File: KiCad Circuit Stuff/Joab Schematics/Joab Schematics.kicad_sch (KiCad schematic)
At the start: 57 parts, among them J1 Conn_02x16_Odd_Even, J2 Conn_01x02, Q1 S8550, Q2 MMBT3904, U1 MT3608, U2 AMS1117-3.3, U3 TP4056, U4 INA219AIDCNR, U6 TS5A3159DCKR, U7 TPS5430DDAR

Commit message: Chose all passive components, added test points to all
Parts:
- removed Q1: S8550, Package_TO_SOT_SMD:SOT-23, symbol Transistor_BJT:S8550
- removed Q2: MMBT3904, Package_TO_SOT_SMD:SOT-23, symbol Transistor_BJT:MMBT3904
- removed R8: 2k, Resistor_SMD:R_0402_1005Metric_Pad0.72x0.64mm_HandSolder, symbol Device:R_Small_US
- removed R9: 1000k, Resistor_SMD:R_0402_1005Metric_Pad0.72x0.64mm_HandSolder, symbol Device:R_Small_US
- removed TP10, TP3, TP4, TP5, TP9: TestPoint, TestPoint:TestPoint_Pad_2.5x2.5mm, symbol Connector:TestPoint
- added 9-5V_R1_TP1: 9-5V R1 TP, TestPoint:TestPoint_Pad_2.5x2.5mm, symbol Connector:TestPoint
- added 9-5V_R2_TP1: 9-5V R2 TP, TestPoint:TestPoint_Pad_2.5x2.5mm, symbol Connector:TestPoint
- added 9-5V_VSense_TP1: 9-5V VSense TP, TestPoint:TestPoint_Pad_2.5x2.5mm, symbol Connector:TestPoint
- added CHRG_SelectR1_TP1, CHRG_SelectR1_TP2, CHRG_SelectR2_TP1, CHRG_SelectR2_TP2, CHRG_VinR_TP1, CHRG_VinR_TP2, Shunt_TP1, Shunt_TP2: TestPoint, TestPoint:TestPoint_Pad_2.5x2.5mm, symbol Connector:TestPoint
- added R16: 2.2k, Resistor_SMD:R_0402_1005Metric_Pad0.72x0.64mm_HandSolder, symbol Device:R_Small_US
- 5V_FB_TP1: renamed from TP7; value TestPoint -> 5V FB TP
- 5V_R1_TP1: renamed from TP6; value TestPoint -> ~
- 5V_R2_TP1: renamed from TP8; value TestPoint -> 5V R2 TP
- L_TP_1: renamed from TP2; value L TP 1 -> ~
- L_TP_2: renamed from TP1; value L TP 2 -> ~
- R10, R11: footprint Resistor_SMD:R_0402_1005Metric_Pad0.72x0.64mm_HandSolder -> Resistor_SMD:R_0603_1608Metric_Pad0.98x0.95mm_HandSolder; LCSC (none) -> C21189
- R12: value 0.1R -> 100m; LCSC (none) -> C7467250
- R13: LCSC (none) -> C4109
- R14: value 5.5k -> 3.3k; LCSC (none) -> C25890
- R15: value 1.5R -> 2.2R; footprint Resistor_SMD:R_0402_1005Metric_Pad0.72x0.64mm_HandSolder -> Resistor_SMD:R_0603_1608Metric_Pad0.98x0.95mm_HandSolder; LCSC (none) -> C22939
- R7: value 5.5k -> 4.7R; footprint Resistor_SMD:R_0402_1005Metric_Pad0.72x0.64mm_HandSolder -> Resistor_SMD:R_0603_1608Metric_Pad0.98x0.95mm_HandSolder; LCSC (none) -> C23164
- renumbered TP13 to 3V3_TP1, TP12 to 5V_TP1, TP11 to 9V_TP1, TP15 to BAT_TP1, TP14 to GND_TP1
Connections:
- net Battery: no longer J1.14 (Pin_14)
- net Battery_In: now also J1.14 (Pin_14), Shunt_TP1.1
- net Battey_Charger_VDD: now also 9-5V_R1_TP1.1
- net GND: now also 9-5V_R2_TP1.1, CHRG_SelectR1_TP2.1, CHRG_SelectR2_TP2.1, CHRG_VinR_TP2.1, R16.2; no longer R14.2
- net at C9.1, R15.1: now also R7.1, CHRG_VinR_TP1.1
- net at R4.1, R5.2, U7.4 (VSENSE): now also 9-5V_VSense_TP1.1
- net at R13.1, U6.1 (NO): now also CHRG_SelectR2_TP1.1
- net at R14.1, U6.3 (NC): now also CHRG_SelectR1_TP1.1
- net Battery_Out renamed Battery_Out_After_Switch
- net Battery_Out_After_Switch: no longer C2.2, JP2.2 (B), R10.1, R12.1, U3.5 (BAT)
- new net: R14.2, R16.1
- new net Battery_Out_Before_Switch: C2.2, JP2.2 (B), R10.1, R12.1, Shunt_TP2.1, U3.5 (BAT)
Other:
- note added: "Notes"
- note removed: "CHANGE THESE RESISTORS"
- note removed: "Cange this resistor"
- note removed: "JOAB YOUR SHIT HERE"
- note removed: "RESISTORS FROM U3-> INA"
- moved on the sheet: 5V_R1_TP1, 5V_R2_TP1, C1, C4, D1, L1, L_TP_1, L_TP_2, R1, R13, R14, R2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

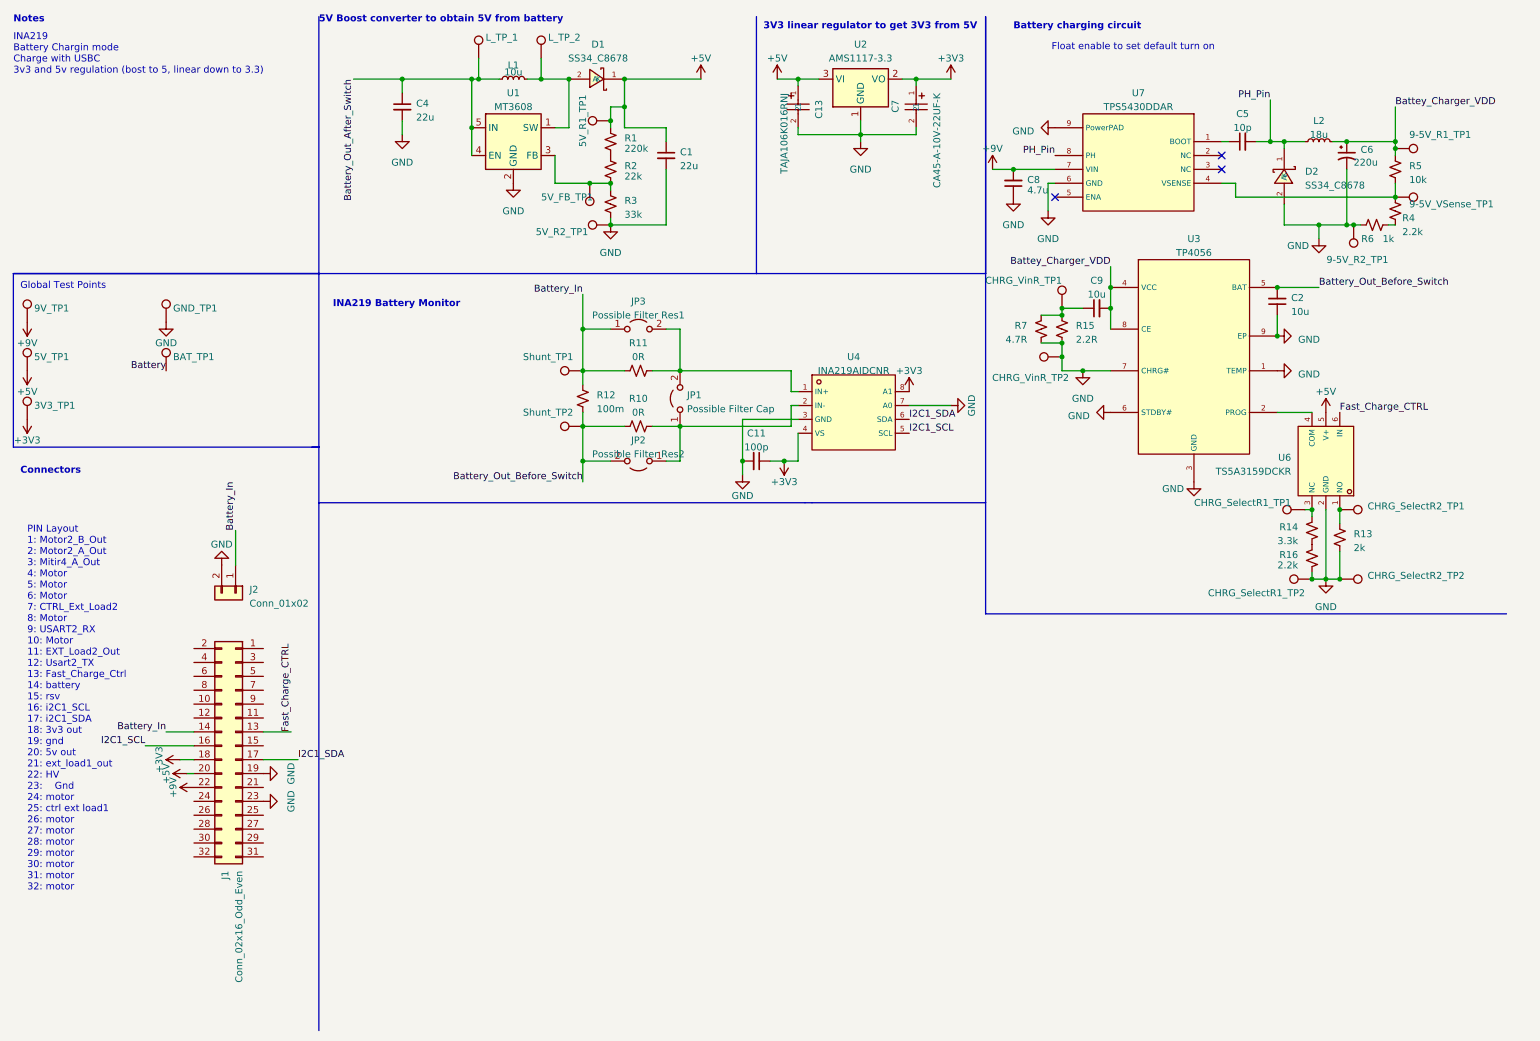
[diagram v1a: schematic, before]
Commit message: Added some lables in Joab Schematic
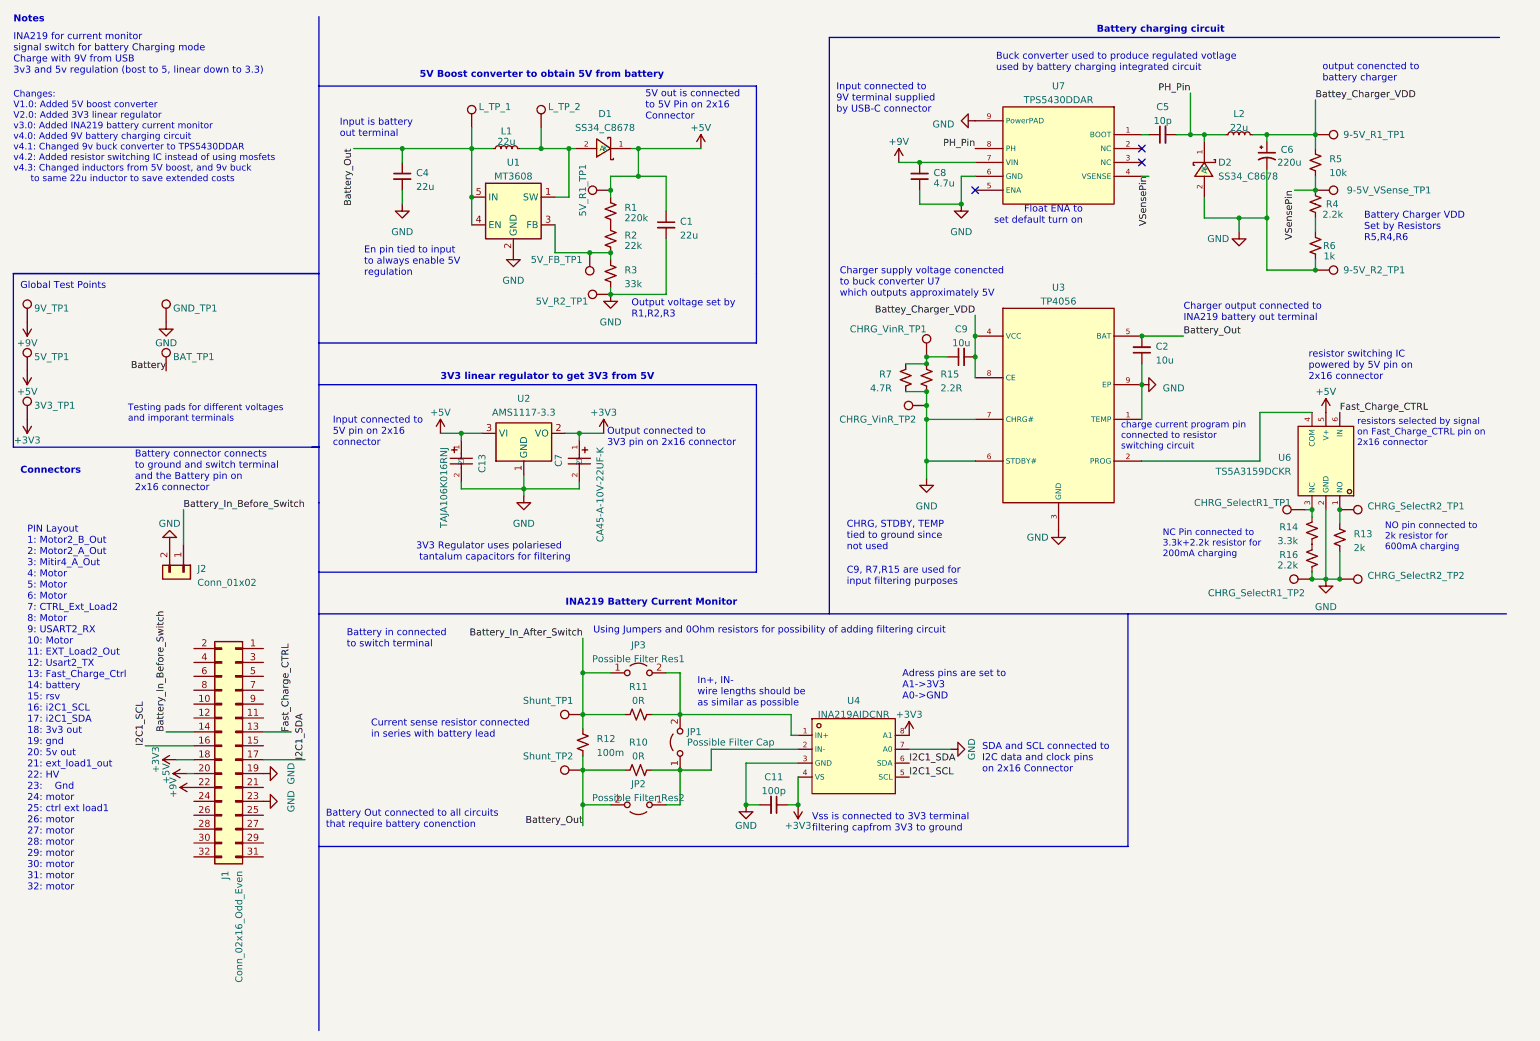
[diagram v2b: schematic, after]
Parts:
- L1: value 10u -> 22u; footprint Inductor_SMD:L_Changjiang_FNR4030S -> Inductor_SMD:L_Sunlord_SWPA6045S; LCSC C167879 -> C83454
- L2: value 18u -> 22u; footprint Inductor_SMD:L_Changjiang_FNR4030S -> Inductor_SMD:L_Sunlord_SWPA6045S; LCSC C167882 -> C83454
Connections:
- net Battery_Out_Before_Switch is gone; now on net Battery_Out: C2.2, JP2.2 (B), R10.1, R12.1, Shunt_TP2.1, U3.5 (BAT)
- net VSensePin: now reaches 9-5V_VSense_TP1.1, R4.1, R5.2, U7.4 (VSENSE)
- net Battery_In renamed Battery_In_After_Switch
- net Battery_In_After_Switch: no longer J1.14 (Pin_14), J2.1 (Pin_1)
- net Battery_Out_After_Switch renamed Battery_Out
- new net Battery_In_Before_Switch: J1.14 (Pin_14), J2.1 (Pin_1)
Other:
- note added: "3V3 Regulator uses polariesed tantalum capacitors for filtering"
- note added: "5V out is connected to 5V Pin on 2x16 Connector"
- note added: "Adress pins are set to A1->3V3 A0->GND"
- note added: "Battery Charger VDD Set by Resistors R5,R4,R6"
- note added: "Battery Out connected to all circuits that require battery conenction"
- note added: "Battery connector connects to ground and switch terminal and the Battery pin on 2x16 connector"
- note added: "Battery in connected to switch terminal"
- note added: "Buck converter used to produce regulated votlage used by battery charging integrated circuit"
- note added: "C9, R7,R15 are used for input filtering purposes"
- note added: "CHRG, STDBY, TEMP tied to ground since not used"
- note added: "Changes: V1.0: Added 5V boost converter V2.0: Added 3V3 linear regulator v3.0: Added INA219 battery current monitor v4.0: Added 9V battery charging circuit v4.1: Changed 9v buck converter to TPS5430DDAR v4.2: Added resistor switching IC instead of using mosfets v4.3: Changed inductors from 5V boost, and 9v buck to same 22u inductor to save extended costs"
- note added: "Charger output connected to INA219 battery out terminal"
- note added: "Charger supply voltage conencted to buck converter U7 which outputs approximately 5V"
- note added: "Current sense resistor connected in series with battery lead"
- note added: "En pin tied to input to always enable 5V regulation"
- note added: "Float ENA to set default turn on"
- note added: "INA219 Battery Current Monitor"
- note added: "INA219 for current monitor signal switch for battery Charging mode Charge with 9V from USB 3v3 and 5v regulation (bost to 5, linear down to 3.3)"
- note added: "In+, IN- wire lengths should be as similar as possible"
- note added: "Input connected to 5V pin on 2x16 connector"
- note added: "Input connected to 9V terminal supplied by USB-C connector"
- note added: "Input is battery out terminal"
- note added: "NC Pin connected to 3.3k+2.2k resistor for 200mA charging"
- note added: "NO pin connected to 2k resistor for 600mA charging"
- note added: "Output connected to 3V3 pin on 2x16 connector"
- note added: "Output voltage set by R1,R2,R3"
- note added: "SDA and SCL connected to I2C data and clock pins on 2x16 Connector"
- note added: "Testing pads for different voltages and imporant terminals"
- note added: "Using Jumpers and 0Ohm resistors for possibility of adding filtering circuit"
- note added: "Vss is connected to 3V3 terminal filtering capfrom 3V3 to ground"
- note added: "charge current program pin connected to resistor switching circuit"
- note added: "output conencted to battery charger"
- note added: "resistor switching IC powered by 5V pin on 2x16 connector"
- note added: "resistors selected by signal on Fast_Charge_CTRL pin on 2x16 connector"
- note removed: "Float enable to set default turn on"
- note removed: "INA219 Battery Chargin mode Charge with USBC 3v3 and 5v regulation (bost to 5, linear down to 3.3)"
- note removed: "INA219 Battery Monitor"
- title: Joab PCP Work -> Joab PCP schematic
- moved on the sheet: 5V_FB_TP1, 5V_R1_TP1, 5V_R2_TP1, 9-5V_R1_TP1, 9-5V_R2_TP1, 9-5V_VSense_TP1, C1, C11, C13, C2, C4, C5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

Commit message: Added ReadMe and other minor changes
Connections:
- net +3V3: now also J1.17 (Pin_17); no longer J1.18 (Pin_18)
- net +5V: now also J1.19 (Pin_19); no longer J1.20 (Pin_20)
- net +9V: now also J1.21 (Pin_21); no longer J1.22 (Pin_22)
- net Battery_In_Before_Switch: now also J1.13 (Pin_13); no longer J1.14 (Pin_14)
- net Fast_Charge_CTRL: now also J1.14 (Pin_14); no longer J1.13 (Pin_13)
- net GND: now also J1.20 (Pin_20), J1.24 (Pin_24); no longer J1.19 (Pin_19), J1.23 (Pin_23)
- net I2C1_SCL: now also J1.15 (Pin_15); no longer J1.16 (Pin_16)
- net I2C1_SDA: now also J1.18 (Pin_18); no longer J1.17 (Pin_17)
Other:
- note added: "PS PIN -> MM PIN Layout NB! Not same as power board pin header 2->1: MOTOR2_B_OUT 1->2: MOTOR2_A_OUT 4->3: MMOTOR4_A_OUT 3->4: MOTOR2_CTRL1 6->5: MOTOR4_B_OUT 5->6: MOTOR2_CTRL2 8->7: CTRL_EXT_LOAD2 7->8: MOTOR4_CTRL1 10->9: USART2_RX 9->10: MOTOR4_CTRL2 12->11: EXT_LOAD2_OUT 11->12: USART2_TX 14->13: FAST_CHARGE_CTRLl 13->14: BATTERY 16->15: RSV 15->16: I2C1_SCL 18->17: I2C1_SDA 17->18: 3V3_OUT 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"
- note removed: "PIN Layout 1: Motor2_B_Out 2: Motor2_A_Out 3: Mitir4_A_Out 4: Motor 5: Motor 6: Motor 7: CTRL_Ext_Load2 8: Motor 9: USART2_RX 10: Motor 11: EXT_Load2_Out 12: Usart2_TX 13: Fast_Charge_Ctrl 14: battery 15: rsv 16: i2C1_SCL 17: i2C1_SDA 18: 3v3 out 19: gnd 20: 5v out 21: ext_load1_out 22: HV 23: Gnd 24: motor 25: ctrl ext load1 26: motor 27: motor 28: motor 29: motor 30: motor 31: motor 32: motor"
- moved on the sheet: J1
